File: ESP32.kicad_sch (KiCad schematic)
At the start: 0 parts

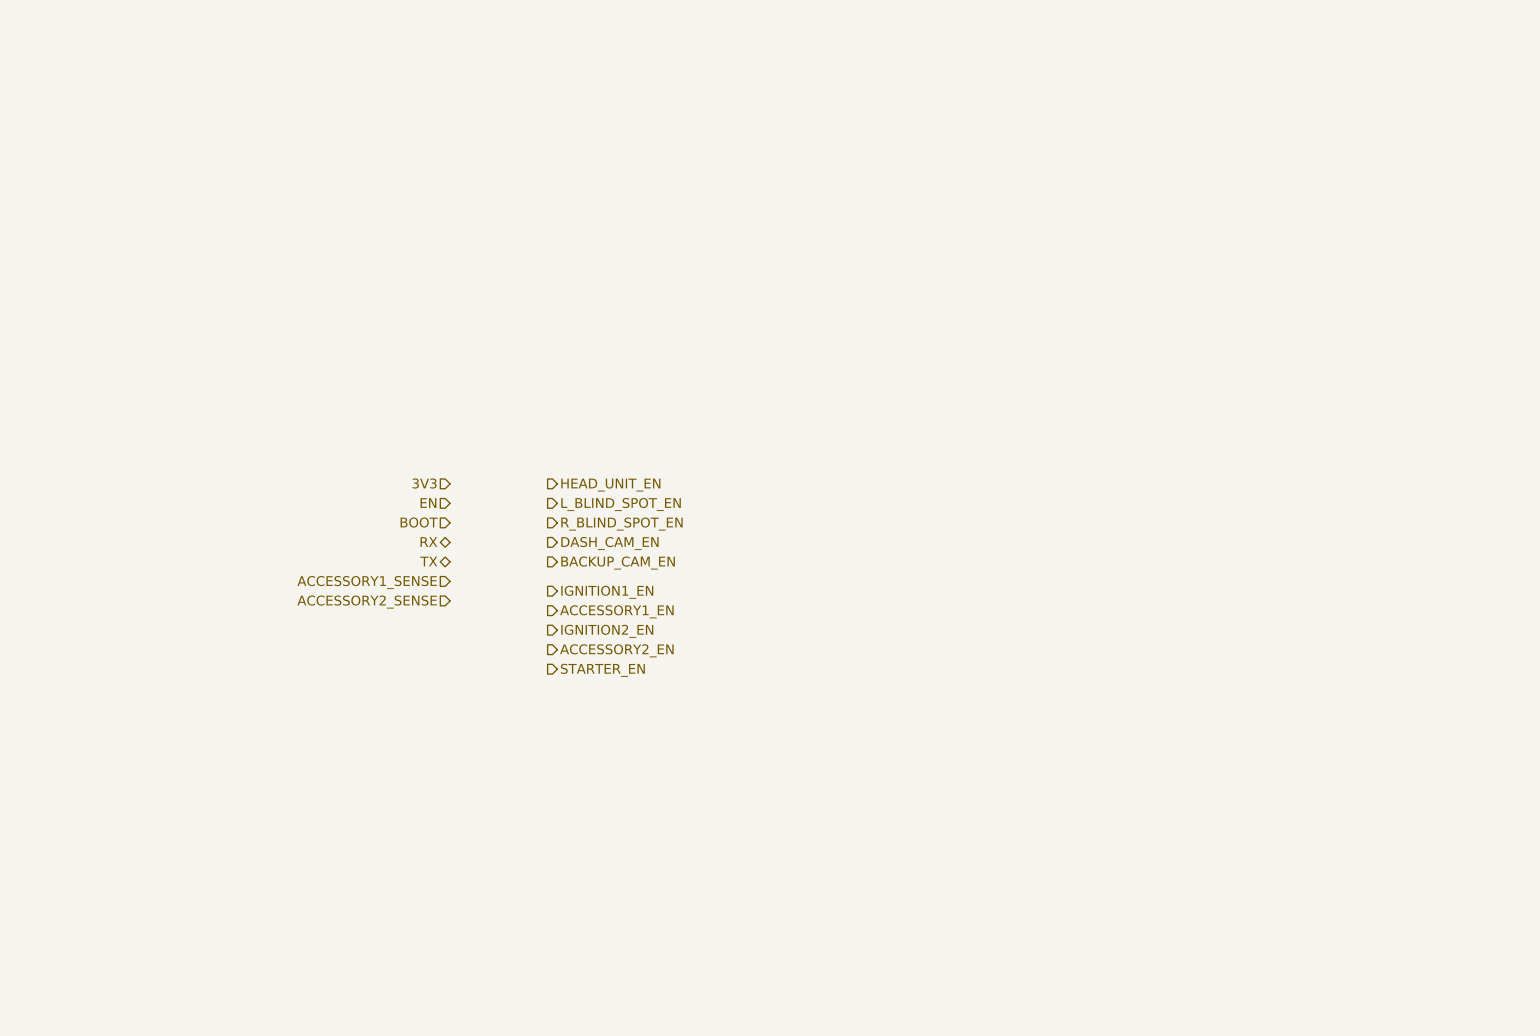
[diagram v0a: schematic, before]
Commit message: power supply circuit schematic done
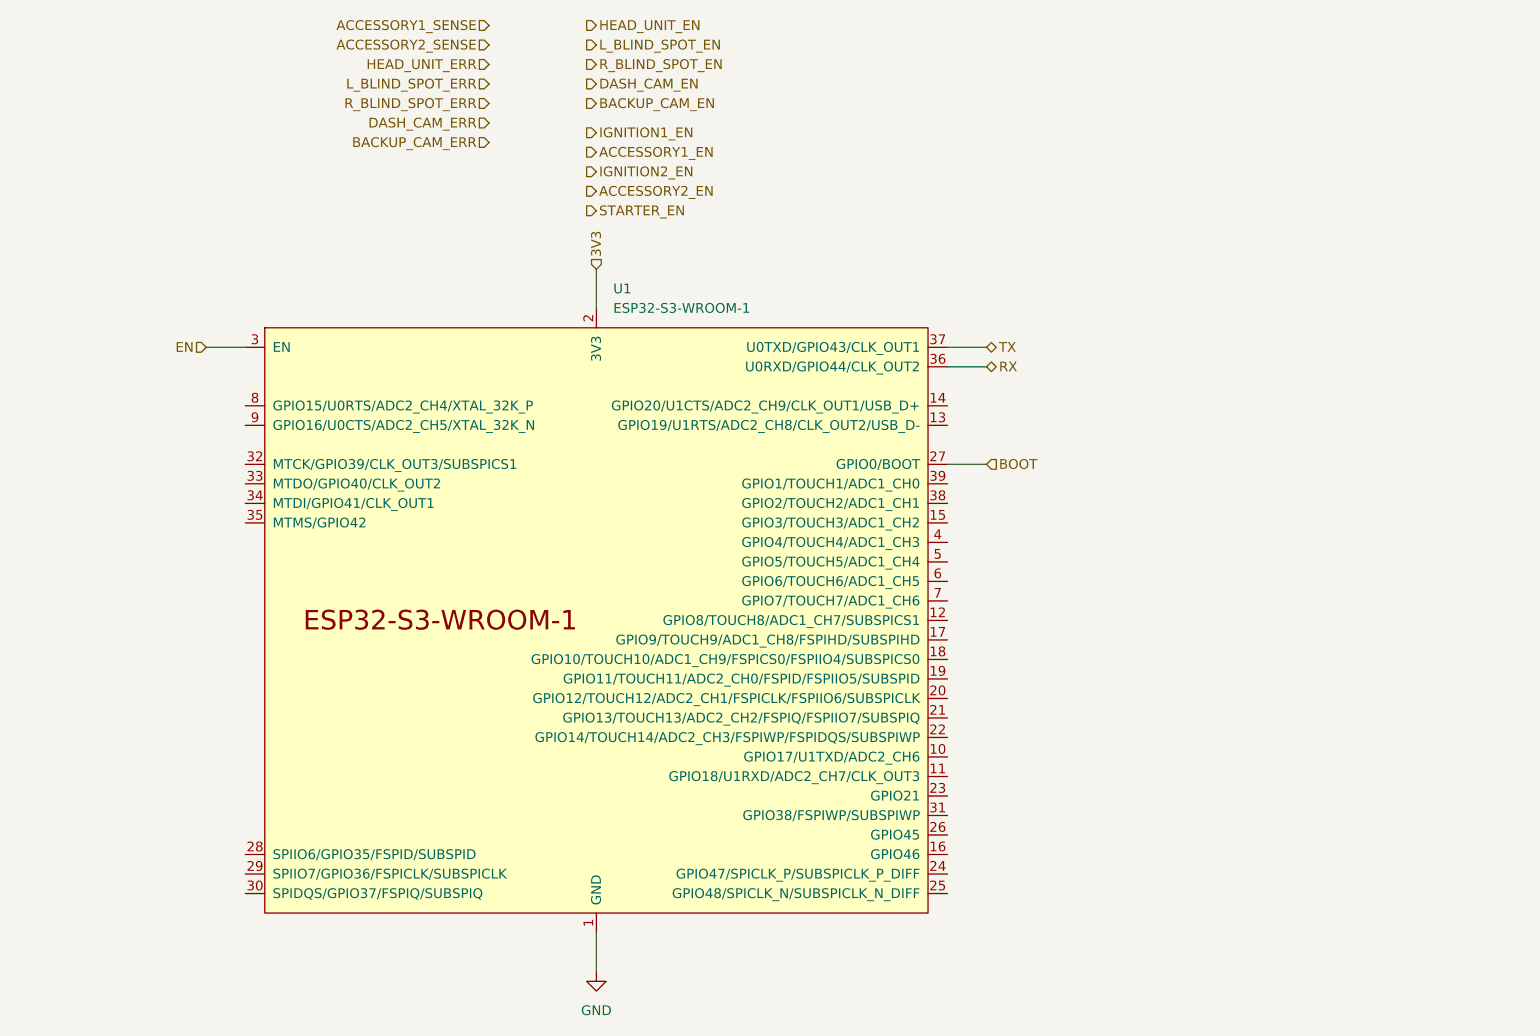
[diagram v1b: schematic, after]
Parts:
- added U1: ESP32-S3-WROOM-1, PCM_Espressif:ESP32-S3-WROOM-1, symbol PCM_Espressif:ESP32-S3-WROOM-1
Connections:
- net 3V3: now also U1.2 (3V3)
- net BOOT: now also U1.27 (GPIO0/BOOT)
- net EN: now also U1.3 (EN)
- net RX: now also U1.36 (U0RXD/GPIO44/CLK_OUT2)
- net TX: now also U1.37 (U0TXD/GPIO43/CLK_OUT1)
- new net GND: U1.1 (GND), U1.40 (GND), U1.41 (GND)
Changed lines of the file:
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@@
     (date "2023-11-22")
   )
-  (hierarchical_label "EN" (shape input) (at 127 91.44 180) (fields_autoplaced)
+  (wire (pts (xy 146.05 147.32) (xy 146.05 152.4))
+    (stroke (width 0) (type default))
+  )
+  (wire (pts (xy 191.77 71.12) (xy 196.85 71.12))
+    (stroke (width 0) (type default))
+  )
+  (wire (pts (xy 95.25 71.12) (xy 100.33 71.12))
+    (stroke (width 0) (type default))
+  )
+  (wire (pts (xy 191.77 73.66) (xy 196.85 73.66))
+    (stroke (width 0) (type default))
+  )
+  (wire (pts (xy 191.77 86.36) (xy 196.85 86.36))
+    (stroke (width 0) (type default))
+  )
+  (wire (pts (xy 146.05 60.96) (xy 146.05 66.04))
+    (stroke (width 0) (type default))
+  )
+  (hierarchical_label "EN" (shape input) (at 95.25 71.12 180) (fields_autoplaced)
     (effects (font (size 1.27 1.27)) (justify right))
   )
-  (hierarchical_label "STARTER_EN" (shape output) (at 139.7 113.03 0) (fields_autoplaced)
+  (hierarchical_label "STARTER_EN" (shape output) (at 144.78 53.34 0) (fields_autoplaced)
     (effects (font (size 1.27 1.27)) (justify left))
   )
-  (hierarchical_label "ACCESSORY2_EN" (shape output) (at 139.7 110.49 0) (fields_autoplaced)
+  (hierarchical_label "ACCESSORY2_EN" (shape output) (at 144.78 50.8 0) (fields_autoplaced)
     (effects (font (size 1.27 1.27)) (justify left))
   )
-  (hierarchical_label "R_BLIND_SPOT_EN" (shape output) (at 139.7 93.98 0) (fields_autoplaced)
+  (hierarchical_label "R_BLIND_SPOT_EN" (shape output) (at 144.78 34.29 0) (fields_autoplaced)
     (effects (font (size 1.27 1.27)) (justify left))
   )
-  (hierarchical_label "BACKUP_CAM_EN" (shape output) (at 139.7 99.06 0) (fields_autoplaced)
+  (hierarchical_label "HEAD_UNIT_ERR" (shape input) (at 132.08 34.29 180) (fields_autoplaced)
+    (effects (font (size 1.27 1.27)) (justify right))
+  )
+  (hierarchical_label "BACKUP_CAM_EN" (shape output) (at 144.78 39.37 0) (fields_autoplaced)
     (effects (font (size 1.27 1.27)) (justify left))
   )
-  (hierarchical_label "ACCESSORY1_SENSE" (shape input) (at 127 101.6 180) (fields_autoplaced)
+  (hierarchical_label "ACCESSORY1_SENSE" (shape input) (at 132.08 29.21 180) (fields_autoplaced)
     (effects (font (size 1.27 1.27)) (justify right))
   )
-  (hierarchical_label "DASH_CAM_EN" (shape output) (at 139.7 96.52 0) (fields_autoplaced)
+  (hierarchical_label "DASH_CAM_EN" (shape output) (at 144.78 36.83 0) (fields_autoplaced)
     (effects (font (size 1.27 1.27)) (justify left))
   )
-  (hierarchical_label "3V3" (shape input) (at 127 88.9 180) (fields_autoplaced)
+  (hierarchical_label "3V3" (shape input) (at 146.05 60.96 90) (fields_autoplaced)
+    (effects (font (size 1.27 1.27)) (justify left))
+  )
+  (hierarchical_label "BOOT" (shape input) (at 196.85 86.36 0) (fields_autoplaced)
+    (effects (font (size 1.27 1.27)) (justify left))
+  )
+  (hierarchical_label "ACCESSORY2_SENSE" (shape input) (at 132.08 31.75 180) (fields_autoplaced)
     (effects (font (size 1.27 1.27)) (justify right))
   )
-  (hierarchical_label "BOOT" (shape input) (at 127 93.98 180) (fields_autoplaced)
+  (hierarchical_label "IGNITION2_EN" (shape output) (at 144.78 48.26 0) (fields_autoplaced)
+    (effects (font (size 1.27 1.27)) (justify left))
+  )
+  (hierarchical_label "L_BLIND_SPOT_ERR" (shape input) (at 132.08 36.83 180) (fields_autoplaced)
     (effects (font (size 1.27 1.27)) (justify right))
   )
-  (hierarchical_label "ACCESSORY2_SENSE" (shape input) (at 127 104.14 180) (fields_autoplaced)
+  (hierarchical_label "RX" (shape bidirectional) (at 196.85 73.66 0) (fields_autoplaced)
+    (effects (font (size 1.27 1.27)) (justify left))
+  )
+  (hierarchical_label "BACKUP_CAM_ERR" (shape input) (at 132.08 44.45 180) (fields_autoplaced)
     (effects (font (size 1.27 1.27)) (justify right))
   )
-  (hierarchical_label "IGNITION2_EN" (shape output) (at 139.7 107.95 0) (fields_autoplaced)
+  (hierarchical_label "IGNITION1_EN" (shape output) (at 144.78 43.18 0) (fields_autoplaced)
     (effects (font (size 1.27 1.27)) (justify left))
   )
-  (hierarchical_label "RX" (shape bidirectional) (at 127 96.52 180) (fields_autoplaced)
+  (hierarchical_label "DASH_CAM_ERR" (shape input) (at 132.08 41.91 180) (fields_autoplaced)
     (effects (font (size 1.27 1.27)) (justify right))
   )
-  (hierarchical_label "IGNITION1_EN" (shape output) (at 139.7 102.87 0) (fields_autoplaced)
+  (hierarchical_label "ACCESSORY1_EN" (shape output) (at 144.78 45.72 0) (fields_autoplaced)
     (effects (font (size 1.27 1.27)) (justify left))
   )
-  (hierarchical_label "ACCESSORY1_EN" (shape output) (at 139.7 105.41 0) (fields_autoplaced)
+  (hierarchical_label "HEAD_UNIT_EN" (shape output) (at 144.78 29.21 0) (fields_autoplaced)
     (effects (font (size 1.27 1.27)) (justify left))
   )
-  (hierarchical_label "HEAD_UNIT_EN" (shape output) (at 139.7 88.9 0) (fields_autoplaced)
+  (hierarchical_label "TX" (shape bidirectional) (at 196.85 71.12 0) (fields_autoplaced)
     (effects (font (size 1.27 1.27)) (justify left))
   )
-  (hierarchical_label "TX" (shape bidirectional) (at 127 99.06 180) (fields_autoplaced)
+  (hierarchical_label "L_BLIND_SPOT_EN" (shape output) (at 144.78 31.75 0) (fields_autoplaced)
+    (effects (font (size 1.27 1.27)) (justify left))
+  )
+  (hierarchical_label "R_BLIND_SPOT_ERR" (shape input) (at 132.08 39.37 180) (fields_autoplaced)
     (effects (font (size 1.27 1.27)) (justify right))
   )
-  (hierarchical_label "L_BLIND_SPOT_EN" (shape output) (at 139.7 91.44 0) (fields_autoplaced)
-    (effects (font (size 1.27 1.27)) (justify left))
+  (symbol (lib_id "power:GND") (at 146.05 152.4 0) (unit 1)
+    (in_bom yes) (on_board yes) (dnp no) (fields_autoplaced)
+    (property "Reference" "#PWR03" (at 146.05 158.75 0)
+      (effects (font (size 1.27 1.27)) hide)
+    )
+    (property "Value" "GND" (at 146.05 157.48 0)
+      (effects (font (size 1.27 1.27)))
+    )
+    (property "Footprint" "" (at 146.05 152.4 0)
+      (effects (font (size 1.27 1.27)) hide)
+    )
+    (property "Datasheet" "" (at 146.05 152.4 0)
+      (effects (font (size 1.27 1.27)) hide)
+    )
+    (pin "1")
+    (instances
+      (project "control-module-pcb"
+        (path "/4c946e98-79c2-4a2d-bd7f-2a33db8d8c91/e59499ee-e888-4aa2-b1ef-f071d9b1365d"
+          (reference "#PWR03") (unit 1)
+        )
+      )
+    )
+  )
+  (symbol (lib_id "PCM_Espressif:ESP32-S3-WROOM-1") (at 146.05 106.68 0) (unit 1)
+    (in_bom yes) (on_board yes) (dnp no)
+    (property "Reference" "U1" (at 148.2441 63.5 0)
+      (effects (font (size 1.27 1.27)) (justify left))
+    )
+    (property "Value" "ESP32-S3-WROOM-1" (at 148.2441 66.04 0)
+      (effects (font (size 1.27 1.27)) (justify left))
+    )
+    (property "Footprint" "PCM_Espressif:ESP32-S3-WROOM-1" (at 148.59 154.94 0)
+      (effects (font (size 1.27 1.27)) hide)
+    )
+    (property "Datasheet" "https://www.espressif.com/sites/default/files/documentation/esp32-s3-wroom-1_wroom-1u_datasheet_en.pdf" (at 148.59 157.48 0)
+      (effects (font (size 1.27 1.27)) hide)
+    )
+    (pin "1")
+    (pin "10")
+    (pin "11")
+    (pin "12")
+    (pin "13")
+    (pin "14")
+    (pin "15")
+    (pin "16")
+    (pin "17")
+    (pin "18")
+    (pin "19")
+    (pin "2")
+    (pin "20")
+    (pin "21")
+    (pin "22")
+    (pin "23")
+    (pin "24")
+    (pin "25")
+    (pin "26")
+    (pin "27")
+    (pin "28")
+    (pin "29")
+    (pin "3")
+    (pin "30")
+    (pin "31")
+    (pin "32")
+    (pin "33")
+    (pin "34")
+    (pin "35")
+    (pin "36")
+    (pin "37")
+    (pin "38")
+    (pin "39")
+    (pin "4")
+    (pin "40")
+    (pin "41")
+    (pin "5")
+    (pin "6")
+    (pin "7")
+    (pin "8")
+    (pin "9")
+    (instances
+      (project "control-module-pcb"
+        (path "/4c946e98-79c2-4a2d-bd7f-2a33db8d8c91/e59499ee-e888-4aa2-b1ef-f071d9b1365d"
+          (reference "U1") (unit 1)
+        )
+      )
+    )
   )
 )

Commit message: assign ESP32 pins
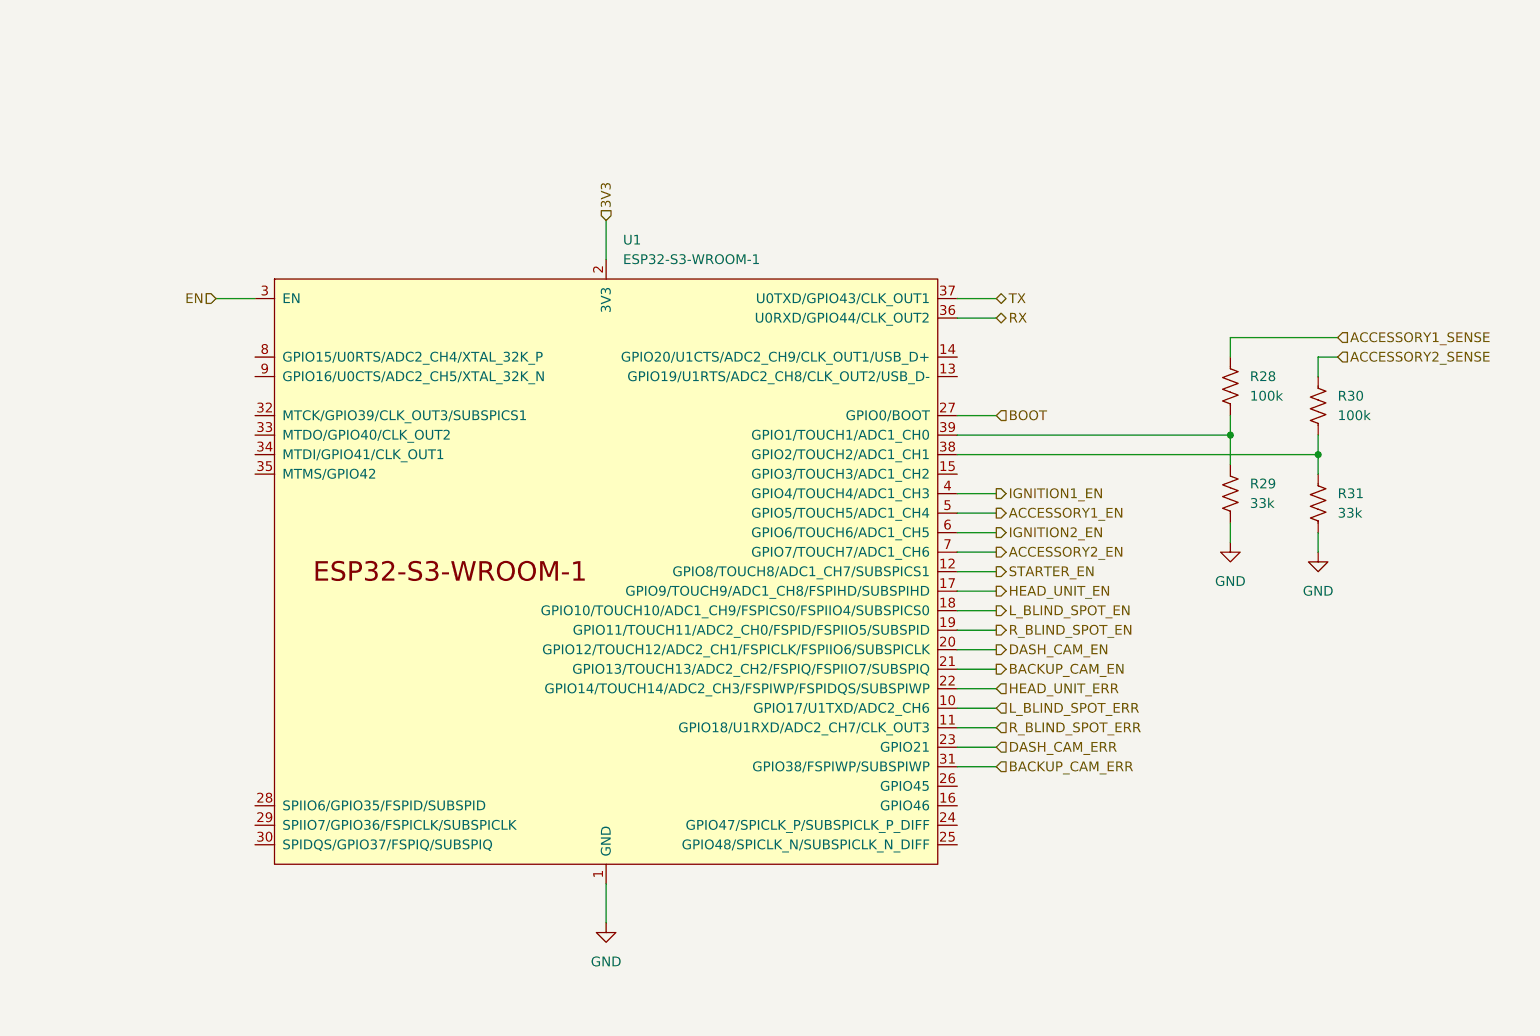
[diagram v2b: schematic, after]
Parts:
- added R28, R30: 100k, symbol Device:R_US
- added R29, R31: 33k, symbol Device:R_US
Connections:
- net ACCESSORY1_EN: now also U1.5 (GPIO5/TOUCH5/ADC1_CH4)
- net ACCESSORY1_SENSE: now also R28.1
- net ACCESSORY2_EN: now also U1.7 (GPIO7/TOUCH7/ADC1_CH6)
- net ACCESSORY2_SENSE: now also R30.1
- net BACKUP_CAM_EN: now also U1.21 (GPIO13/TOUCH13/ADC2_CH2/FSPIQ/FSPIIO7/SUBSPIQ)
- net BACKUP_CAM_ERR: now also U1.31 (GPIO38/FSPIWP/SUBSPIWP)
- net DASH_CAM_EN: now also U1.20 (GPIO12/TOUCH12/ADC2_CH1/FSPICLK/FSPIIO6/SUBSPICLK)
- net DASH_CAM_ERR: now also U1.23 (GPIO21)
- net GND: now also R29.2, R31.2
- net HEAD_UNIT_EN: now also U1.17 (GPIO9/TOUCH9/ADC1_CH8/FSPIHD/SUBSPIHD)
- net HEAD_UNIT_ERR: now also U1.22 (GPIO14/TOUCH14/ADC2_CH3/FSPIWP/FSPIDQS/SUBSPIWP)
- net IGNITION1_EN: now also U1.4 (GPIO4/TOUCH4/ADC1_CH3)
- net IGNITION2_EN: now also U1.6 (GPIO6/TOUCH6/ADC1_CH5)
- net L_BLIND_SPOT_EN: now also U1.18 (GPIO10/TOUCH10/ADC1_CH9/FSPICS0/FSPIIO4/SUBSPICS0)
- net L_BLIND_SPOT_ERR: now also U1.10 (GPIO17/U1TXD/ADC2_CH6)
- net R_BLIND_SPOT_EN: now also U1.19 (GPIO11/TOUCH11/ADC2_CH0/FSPID/FSPIIO5/SUBSPID)
- net R_BLIND_SPOT_ERR: now also U1.11 (GPIO18/U1RXD/ADC2_CH7/CLK_OUT3)
- net STARTER_EN: now also U1.12 (GPIO8/TOUCH8/ADC1_CH7/SUBSPICS1)
- net at U1.38 (GPIO2/TOUCH2/ADC1_CH1): now also R30.2, R31.1
- net at U1.39 (GPIO1/TOUCH1/ADC1_CH0): now also R28.2, R29.1
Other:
- moved on the sheet: U1
